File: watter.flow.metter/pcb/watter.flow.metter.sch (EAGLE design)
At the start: 21 parts, among them Q1 BC546A

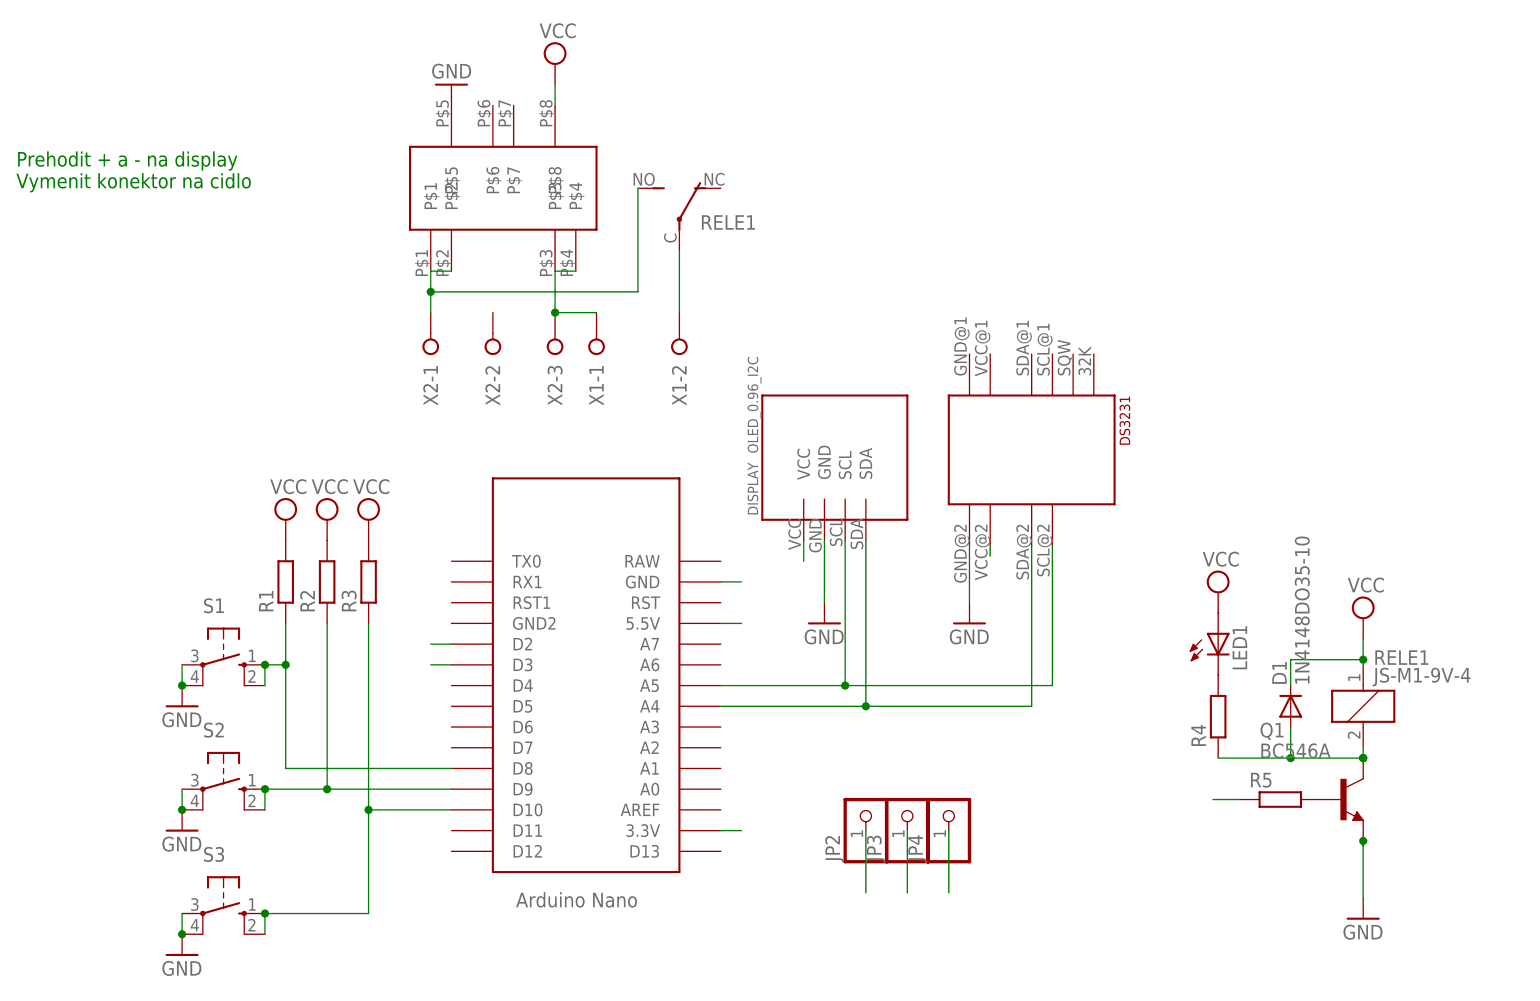
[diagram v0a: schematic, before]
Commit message: add timer for periodical switching relay
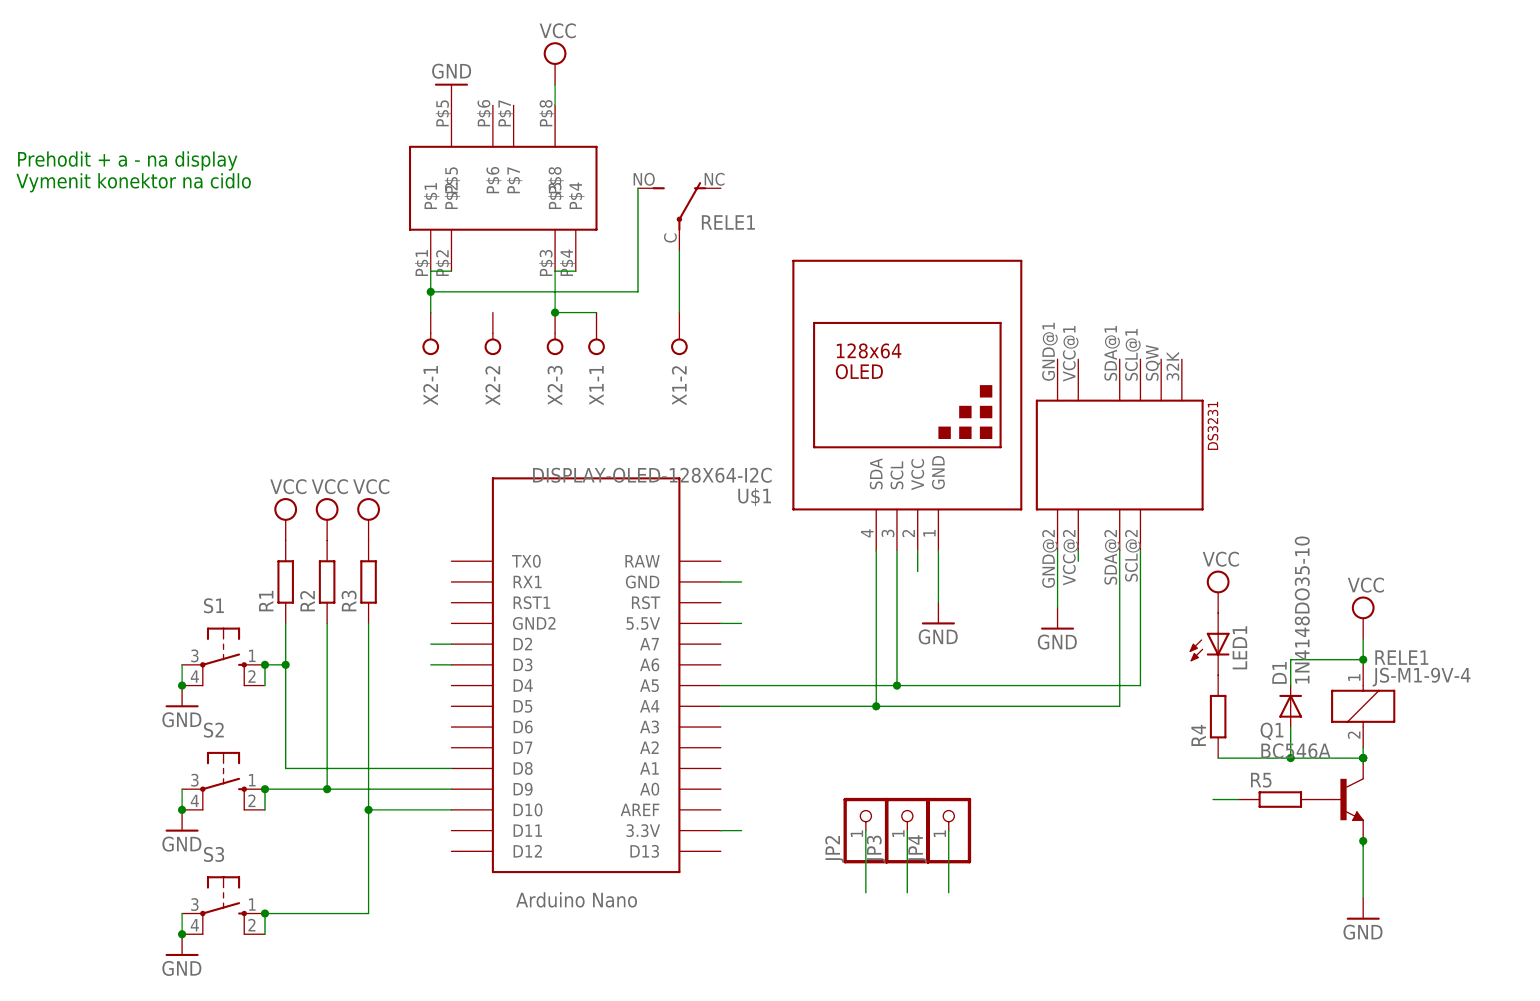
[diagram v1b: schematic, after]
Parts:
- removed DISPLAY: OLED_0.96_I2C, tft_1.8_1.44_oled_0.96:OLED_0.96_I2C
- added U$1: DISPLAY-OLED-128X64-I2C, diy-modules:DISPLAY-OLED-128X64-I2C
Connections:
- net 3.3V: now also U$1.VCC; no longer DISPLAY.VCC
- net GND: now also U$1.GND; no longer DISPLAY.GND
- net SCL: now also U$1.SCL; no longer DISPLAY.SCL
- net SDA: now also U$1.SDA; no longer DISPLAY.SDA
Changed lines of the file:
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@@
 <part name="U$5" library="Arduino" deviceset="NANO" device=""/>
 <part name="GND16" library="supply1" library_urn="urn:adsk.eagle:library:371" deviceset="GND" device=""/>
-<part name="DISPLAY" library="tft_1.8_1.44_oled_0.96" deviceset="OLED_0.96_I2C" device=""/>
 <part name="RELE1" library="relay" library_urn="urn:adsk.eagle:library:339" deviceset="JS-M1*" device="" technology="-9V-4"/>
 <part name="X1" library="con-wago-508" library_urn="urn:adsk.eagle:library:196" deviceset="W237-02P" device=""/>
@@
 <part name="LED1" library="led" library_urn="urn:adsk.eagle:library:259" deviceset="LED" device="3MM"/>
 <part name="R4" library="rcl" library_urn="urn:adsk.eagle:library:334" deviceset="R-EU_" device="0207/10"/>
+<part name="U$1" library="diy-modules" deviceset="DISPLAY-OLED-128X64-I2C" device=""/>
 </parts>
 <sheets>
@@
 <instances>
 <instance part="U$5" gate="G$1" x="5.08" y="48.26" rot="R180"/>
-<instance part="GND16" gate="1" x="40.64" y="60.96"/>
-<instance part="DISPLAY" gate="G$1" x="43.18" y="81.28"/>
+<instance part="GND16" gate="1" x="54.61" y="60.96"/>
 <instance part="RELE1" gate="1" x="106.68" y="50.8"/>
 <instance part="RELE1" gate="2" x="22.86" y="109.22"/>
@@
 <instance part="GND13" gate="1" x="106.68" y="24.765"/>
 <instance part="R5" gate="G$1" x="96.52" y="39.37"/>
-<instance part="U$6" gate="G$1" x="55.88" y="88.9" rot="R270"/>
+<instance part="U$6" gate="G$1" x="66.675" y="88.265" rot="R270"/>
 <instance part="S1" gate="1" x="-33.02" y="55.88" rot="R270"/>
 <instance part="S2" gate="1" x="-33.02" y="40.64" rot="R270"/>
@@
 <instance part="GND1" gate="1" x="-5.08" y="127" rot="R180"/>
 <instance part="SUPPLY1" gate="G$1" x="7.62" y="129.54"/>
-<instance part="GND2" gate="1" x="58.42" y="60.96"/>
+<instance part="GND2" gate="1" x="69.215" y="60.325"/>
 <instance part="GND3" gate="1" x="-38.1" y="50.8"/>
 <instance part="GND4" gate="1" x="-38.1" y="35.56"/>
@@
 <instance part="LED1" gate="G$1" x="88.9" y="59.69"/>
 <instance part="R4" gate="G$1" x="88.9" y="49.53" rot="R90"/>
+<instance part="U$1" gate="G$1" x="49.53" y="90.17" rot="R180"/>
 </instances>
 <busses>
@@
 <net name="GND" class="0">
 <segment>
-<pinref part="DISPLAY" gate="G$1" pin="GND"/>
 <pinref part="GND16" gate="1" pin="GND"/>
-<wire x1="40.64" y1="63.5" x2="40.64" y2="71.12" width="0.1524" layer="91"/>
+<wire x1="54.61" y1="63.5" x2="54.61" y2="69.85" width="0.1524" layer="91"/>
+<pinref part="U$1" gate="G$1" pin="GND"/>
 </segment>
 <segment>
@@
 <pinref part="U$6" gate="G$1" pin="GND@2"/>
 <pinref part="GND2" gate="1" pin="GND"/>
-<wire x1="58.42" y1="63.5" x2="58.42" y2="70.485" width="0.1524" layer="91"/>
+<wire x1="69.215" y1="62.865" x2="69.215" y2="69.85" width="0.1524" layer="91"/>
 </segment>
 </net>
@@
 <segment>
 <pinref part="U$5" gate="G$1" pin="A4"/>
-<wire x1="27.94" y1="50.8" x2="45.72" y2="50.8" width="0.1524" layer="91"/>
-<pinref part="DISPLAY" gate="G$1" pin="SDA"/>
-<wire x1="45.72" y1="50.8" x2="45.72" y2="71.12" width="0.1524" layer="91"/>
-<wire x1="66.04" y1="70.485" x2="66.04" y2="50.8" width="0.1524" layer="91"/>
-<wire x1="66.04" y1="50.8" x2="45.72" y2="50.8" width="0.1524" layer="91"/>
-<junction x="45.72" y="50.8"/>
+<wire x1="27.94" y1="50.8" x2="46.99" y2="50.8" width="0.1524" layer="91"/>
+<wire x1="46.99" y1="50.8" x2="46.99" y2="69.85" width="0.1524" layer="91"/>
+<wire x1="76.835" y1="69.85" x2="76.835" y2="50.8" width="0.1524" layer="91"/>
+<wire x1="76.835" y1="50.8" x2="46.99" y2="50.8" width="0.1524" layer="91"/>
+<junction x="46.99" y="50.8"/>
 <pinref part="U$6" gate="G$1" pin="SDA@2"/>
+<pinref part="U$1" gate="G$1" pin="SDA"/>
 </segment>
 </net>
@@
 <segment>
 <pinref part="U$5" gate="G$1" pin="A5"/>
-<pinref part="DISPLAY" gate="G$1" pin="SCL"/>
-<wire x1="43.18" y1="71.12" x2="43.18" y2="53.34" width="0.1524" layer="91"/>
-<wire x1="43.18" y1="53.34" x2="27.94" y2="53.34" width="0.1524" layer="91"/>
-<wire x1="43.18" y1="53.34" x2="68.58" y2="53.34" width="0.1524" layer="91"/>
-<wire x1="68.58" y1="53.34" x2="68.58" y2="70.485" width="0.1524" layer="91"/>
-<junction x="43.18" y="53.34"/>
+<wire x1="49.53" y1="69.85" x2="49.53" y2="53.34" width="0.1524" layer="91"/>
+<wire x1="49.53" y1="53.34" x2="27.94" y2="53.34" width="0.1524" layer="91"/>
+<wire x1="49.53" y1="53.34" x2="79.375" y2="53.34" width="0.1524" layer="91"/>
+<wire x1="79.375" y1="53.34" x2="79.375" y2="69.85" width="0.1524" layer="91"/>
+<junction x="49.53" y="53.34"/>
 <pinref part="U$6" gate="G$1" pin="SCL@2"/>
+<pinref part="U$1" gate="G$1" pin="SCL"/>
 </segment>
 </net>
@@
 <segment>
 <pinref part="U$6" gate="G$1" pin="VCC@2"/>
-<wire x1="60.96" y1="69.215" x2="60.96" y2="70.485" width="0.1524" layer="91"/>
-</segment>
-<segment>
-<pinref part="DISPLAY" gate="G$1" pin="VCC"/>
-<wire x1="38.1" y1="68.58" x2="38.1" y2="71.12" width="0.1524" layer="91"/>
-</segment>
-</net>
+<wire x1="71.755" y1="68.58" x2="71.755" y2="69.85" width="0.1524" layer="91"/>
+</segment>
+<segment>
+<wire x1="52.07" y1="67.31" x2="52.07" y2="69.85" width="0.1524" layer="91"/>
+<pinref part="U$1" gate="G$1" pin="VCC"/>
+</segment>
+</net>
